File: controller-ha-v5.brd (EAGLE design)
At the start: 120 x 75 mm, 29 parts, among them IC2 LM358MX, U1 DS1307

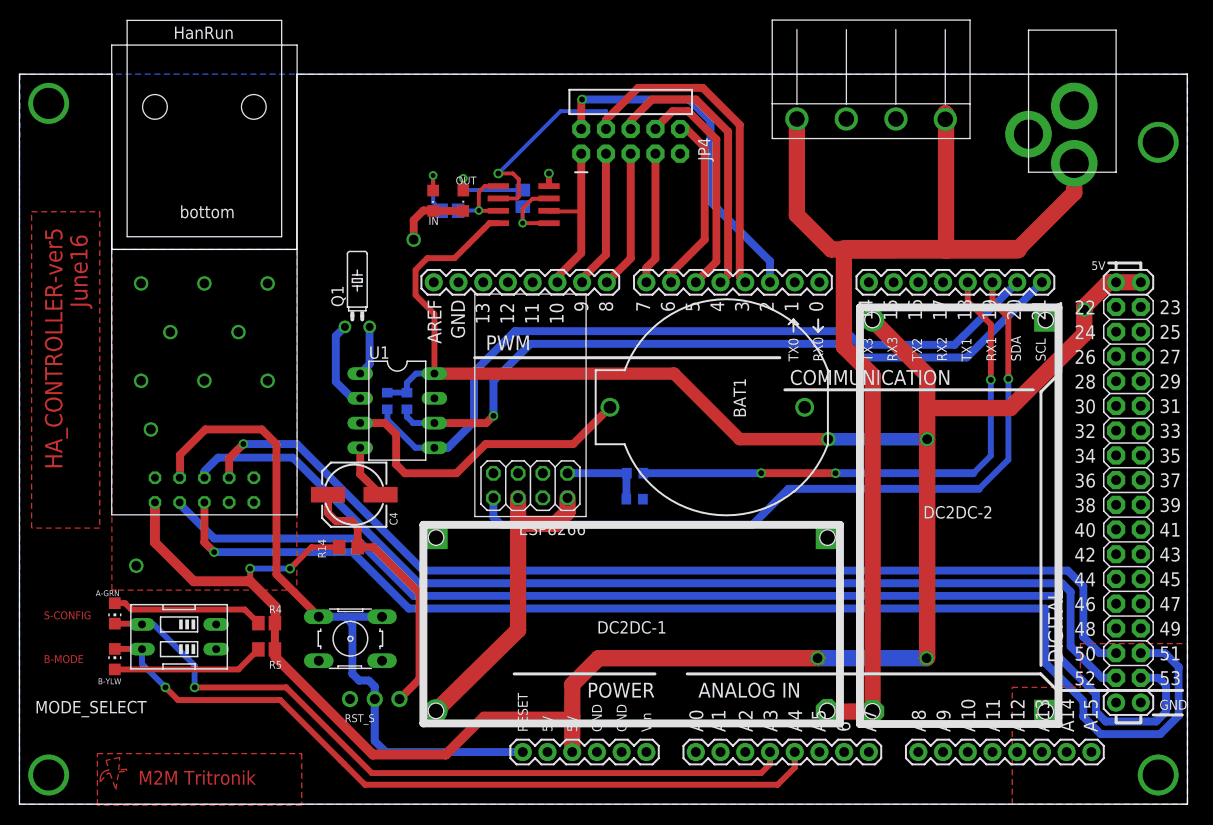
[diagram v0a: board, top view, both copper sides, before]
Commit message: autoroute
remove gnd plane, add gnd route
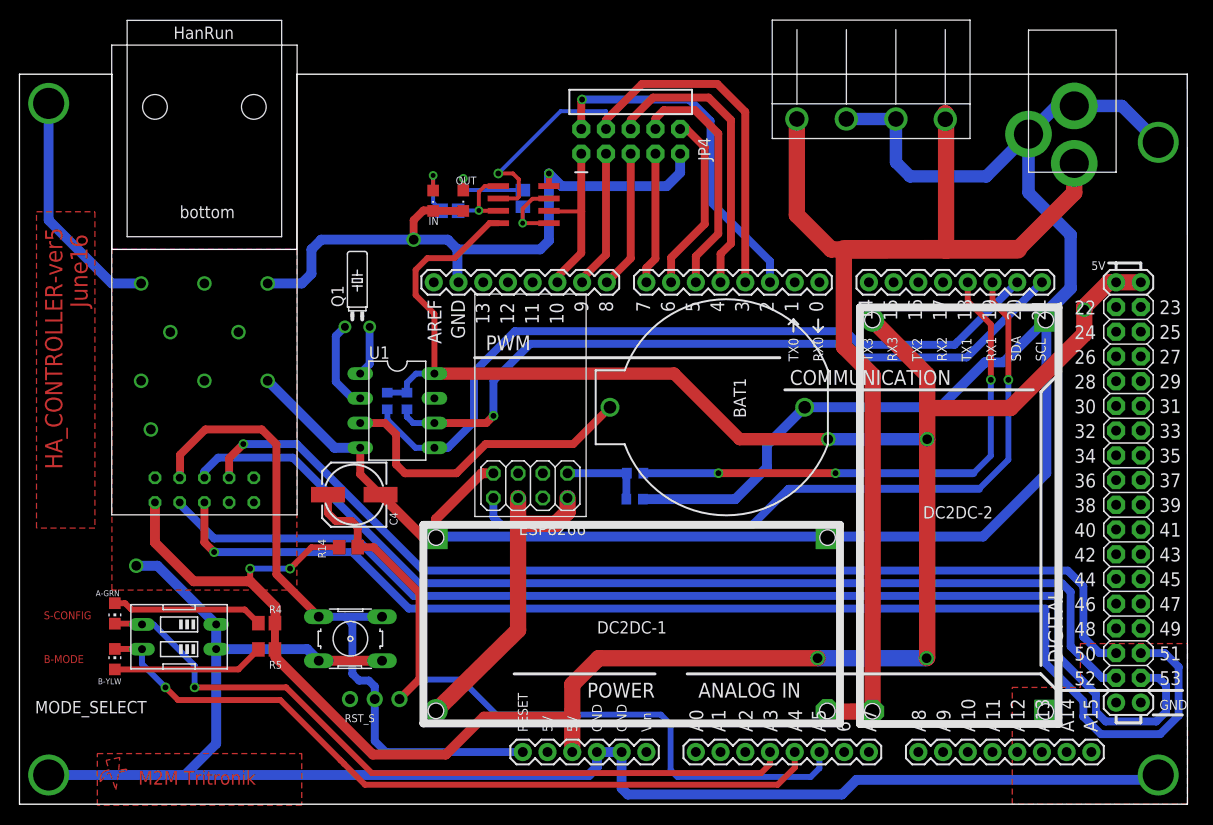
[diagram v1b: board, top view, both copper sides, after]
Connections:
- net AUTORESET: now also ARDUINO_FOOTPRINT.A5
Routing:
- net GND: track 14.5 -> 489.3 mm
- net AUTORESET: track 27.7 -> 80.6 mm
- net SR_DS: track 55.9 -> 57.3 mm
- net SHCP: track 23.8 -> 25.2 mm
- net STCP: track 28.9 -> 30.3 mm
- removed copper zone on layer 16, net GND

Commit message: Upgrade to version 5
With LAN Ethernet ENC28J60; adding relay for restarting 12V modules
(Driver & IO).
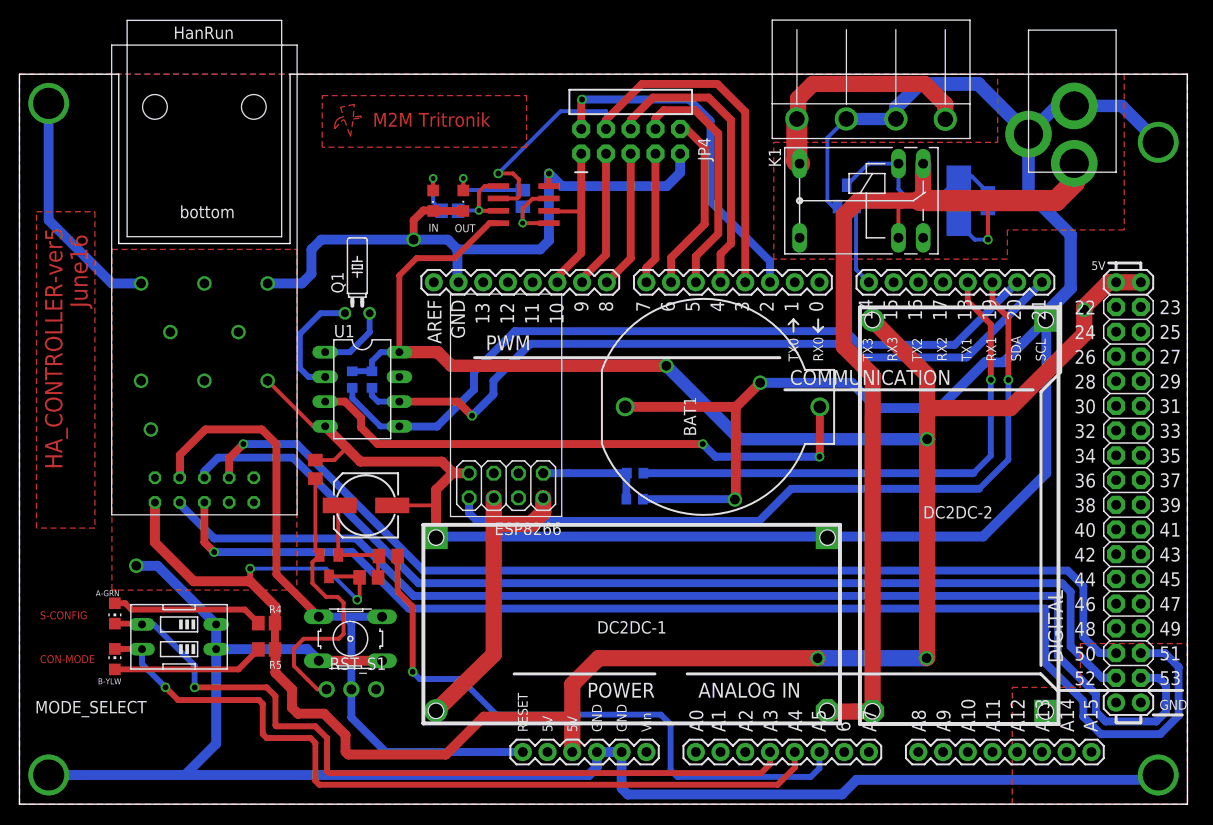
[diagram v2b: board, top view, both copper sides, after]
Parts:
- removed C4: 100uF 35V, resistor:153CLV-0605
- removed R14: 120k, rcl:R0805
- removed RST_S: (no value), adafruit:1X03-CLEANBIG
- added C5: 100uF 16V, resistor:153CLV-0605
- added D1: (no value), adafruit:SMADIODE
- added K1: M3XXH, relay:M3XXH
- added R16: 120k, rcl:R0805
- added R17: 10k, rcl:R0805
- added R18: 1k, rcl:R0805
- added R2: 10K, resistor:R0805
- added RST_S1: (no value), adafruit:1X03-CLEANBIG
- added T2, T3: (no value), transistor:SOT23-BEC
- moved R2K2_SCL 4.22 mm to (36.2, 43.6)
- moved R2K2_SDA 4.22 mm to (34.2, 43.6)
- moved U1 4.22 mm to (35.2, 42.6)
- moved ESP8266 2.50 mm to (50.0, 32.7)
- moved BAT1 2.14 mm to (70.4, 40.8), turned to 0 degrees
- moved Q1 1.40 mm to (34.7, 50.4)
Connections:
- new net DRV_ON: ARDUINO_FOOTPRINT.14, T2.B
- new net N$3: 4-WAY_L-TERMINAL.1, 4-WAY_L-TERMINAL.4, K1.P
- new net N$4: D1.A, K1.2, R2.1, T2.C
- new net N$5: R17.2, RST_S1.3, T3.E
- new net NET1: C5.+, R16.1, R18.2, T3.B
- net +12V: now also D1.C, K1.1, K1.O, R2.2; no longer 4-WAY_L-TERMINAL.1, 4-WAY_L-TERMINAL.4
- net AUTORESET: now also R18.1; no longer C4.+, R14.1, RST_S.3
- net GND: now also C5.-, R17.1, T2.E; no longer C4.-
- net NC: now also RST_S1.1; no longer RST_S.1
- net RST: now also RST_S1.2; no longer RST_S.2
- net VCC: now also R16.2, T3.C; no longer R14.2
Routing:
- net GND: track 489.3 -> 520.1 mm, vias 16 -> 18
- net N$5: track 0.00 -> 30.4 mm
- net N$23: track 32.4 -> 58.9 mm, vias 0 -> 2
- net N$3: track 0.00 -> 25.0 mm
- net N$4: track 0.00 -> 20.8 mm
- net AUTORESET: track 80.6 -> 63.6 mm, vias 0 -> 1
- net VCC: track 264.3 -> 278.1 mm
- net NET1: track 0.00 -> 12.2 mm
- net +12V: track 114.2 -> 102.6 mm, vias 0 -> 1
- net DRV_ON: track 0.00 -> 8.33 mm
- net STATE_B: track 78.9 -> 83.0 mm
- net STATE_A: track 76.6 -> 80.4 mm
- net N$16: track 9.24 -> 12.0 mm
- net SCL: track 75.6 -> 78.2 mm
- net ESP_RX: track 8.78 -> 11.3 mm
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- added copper zone on layer 16, net GND
- added copper zone on layer 1, net N$6
- added copper zone on layer 1, net N$8
- added copper zone on layer 1, net TRITRONIK1
- removed copper zone on layer 1, net N$18
- removed copper zone on layer 1, net TRITRONIK
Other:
- outline, holes or cut-outs redrawn
- board text added: "CON-MODE"
- board text removed: "B-MODE"
